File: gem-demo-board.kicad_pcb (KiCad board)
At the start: 6 copper layers, 56 x 66 mm, 153 parts, among them J1 3220-10-0100-00, J10 0473460001, J2 DF13A-2P-1.25H, J3 3220-10-0100-00, J4 2x20_Header_Female, J5 0473460001, J6 556500488, J7 556500488, J8 WE_686115148922_FLIPPED, J9 WE_686115148922_FLIPPED, U1 MCP1700T-3302E_TT, U2 NTS0104BQ, U3 NTS0104BQ, U4 NTS0104BQ, U5 93LC56CT-IMC, U6 FT4232HQ, U7 NTB0104BQ, U8 NTB0104BQ, Y1 ASFLMB-12.000MHZ-LC-T

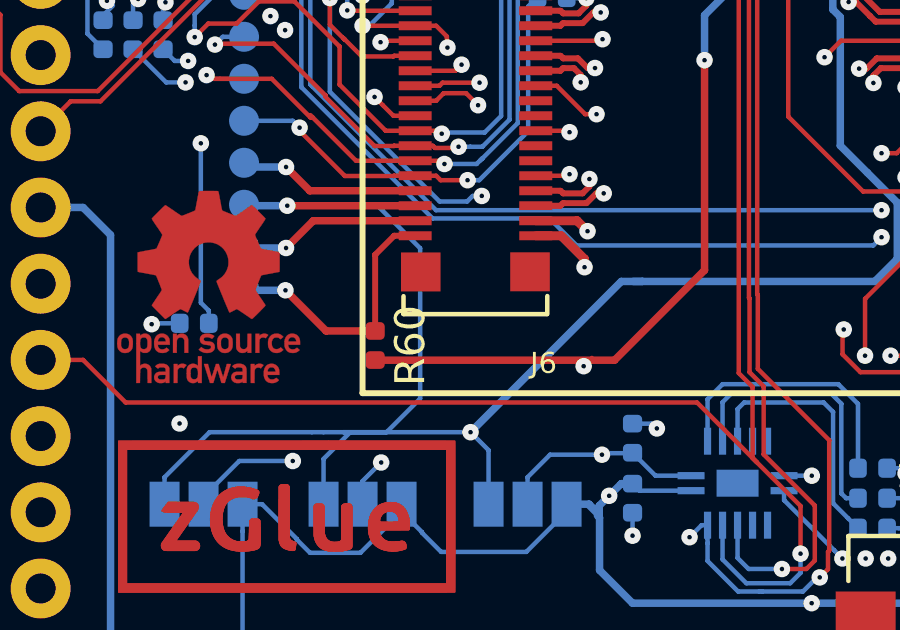
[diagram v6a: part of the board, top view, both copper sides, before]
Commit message: Cleanup of DRC issues
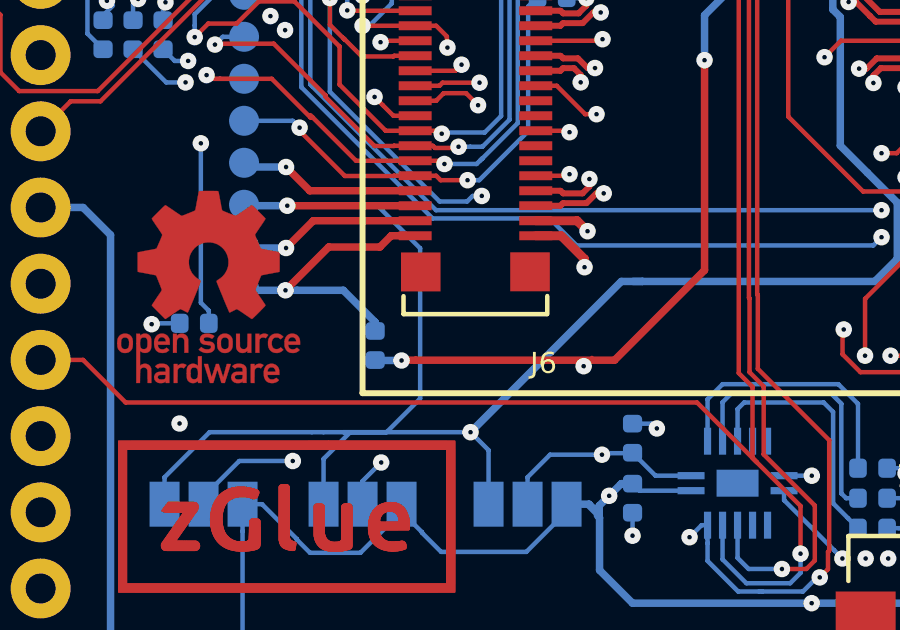
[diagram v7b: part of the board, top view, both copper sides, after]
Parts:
- R60: moved to B.Cu
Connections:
- C21 pad 1: Net-(C21-Pad1) -> /VPHY
- C22 pad 1: Net-(C22-Pad1) -> /VPLL
- C25 pad 1: Net-(C25-Pad1) -> /VPHY
- C26 pad 1: Net-(C26-Pad1) -> /VPLL
- D10 pad 1: Net-(D10-Pad1) -> /3V3_SYS
- D11 pad 1: Net-(D11-Pad1) -> /3V3_SYS
- D8 pad 1: Net-(D8-Pad1) -> /3V3_SYS
- D9 pad 1: Net-(D9-Pad1) -> /3V3_SYS
- R4 pad 2: Net-(R4-Pad2) -> /3V3_FTDI
- R42 pad 2: /RPI_DBG_RX_3V3 -> /DBG_TX_3V3
- R43 pad 2: /RPI_DBG_TX_3V3 -> /DBG_RX_3V3
- R50 pad 2: /I2C_0_SCL_3V3 -> /I2C_0_SDA_3V3
- R51 pad 2: /I2C_0_SDA_3V3 -> /I2C_0_SCL_3V3
- R52 pad 2: /CAM_SCL_IN -> /CAM_SDA_IN
- R53 pad 2: /CAM_SDA_IN -> /CAM_SCL_IN
- R56 pad 2: /CAM_SCL_IN -> /CAM_SDA_IN
- R57 pad 2: /CAM_SDA_IN -> /CAM_SCL_IN
- R6 pad 2: Net-(R6-Pad2) -> /3V3_FTDI
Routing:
- net /CSI_D1_IN_P: track 43.0 -> 45.0 mm
- net Net-(J6-Pad40): track 9.09 -> 10.2 mm
- net /3V3_SYS: vias 20 -> 21
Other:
- board text removed: "Rev. 1.1 11/2019"

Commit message: Minor updates on PCB
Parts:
- R58, R59: footprint zglue-demo-board-footprints:0402-res -> gem-demo-board-footprints:0402-res
- moved R58 9.28 mm to (73.6, 38.6), turned to 0 degrees
- moved R59 8.81 mm to (73.6, 39.9), turned to 0 degrees
- renumbered D6 to PWR
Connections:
- R58 pad 1: /RPI_DBG_RX_3V3 -> /CAM_SDA_IN
- R58 pad 2: /DBG_TX_3V3 -> /CAM_SDA_OUT
- R59 pad 1: /RPI_DBG_TX_3V3 -> /CAM_SCL_IN
- R59 pad 2: /DBG_RX_3V3 -> /CAM_SCL_OUT
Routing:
- net Net-(U6-Pad48): track 18.6 -> 0.00 mm, vias 2 -> 0
- net /3V3_SYS: track 246.2 -> 227.7 mm, vias 21 -> 20
- net /I2C_0_SDA_3V3: track 16.9 -> 25.8 mm
- net /RPI_DBG_RX_3V3: track 6.54 -> 0.00 mm, vias 2 -> 0
- net /RPI_DBG_TX_3V3: track 6.16 -> 0.00 mm
- net /DBG_RX_3V3: track 38.1 -> 33.1 mm
- net /CAM_SDA_IN: track 90.3 -> 95.2 mm, vias 4 -> 3
- net /I2C_0_SCL_3V3: track 28.3 -> 24.9 mm
- net /CAM_SCL_IN: track 73.4 -> 76.5 mm, vias 2 -> 3
- net /CAM_SDA_OUT: track 17.6 -> 19.8 mm, vias 2 -> 3
- net /DBG_TX_3V3: track 32.3 -> 30.1 mm, vias 4 -> 5
- net /CAM_SCL_OUT: track 18.5 -> 20.1 mm, vias 2 -> 3
